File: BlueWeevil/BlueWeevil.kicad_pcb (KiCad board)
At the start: 2 copper layers, 370.5 x 94.4 mm, 256 parts, among them U1 Teensy_3.2, U2 AN32183A

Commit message: 1st pass at layout. Needs packages verified, and underglow LEDs added
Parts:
- removed the CHERRY at (331.0, 85.7)
- removed the CHERRY at (92.9, 85.7)
- removed the CHERRY at (335.8, 66.7)
- removed the REF** at (379.5, 76.5)
- removed the REF** at (314.3, 66.7)
- removed the REF** at (381.0, 67.3)
- removed the REF** at (375.3, 67.3)
- removed the REF** at (370.2, 67.3)
- removed the REF** at (361.3, 67.3)
- removed the REF** at (353.5, 75.4)
- removed the REF** at (74.9, 66.7)
- removed the REF** at (361.9, 28.6)
- removed the REF** at (362.6, 47.6)
- removed the REF** at (392.0, 76.5)
- removed the REF** at (358.8, 47.6)
- removed the REF** at (387.0, 76.5)
- removed the REF** at (203.8, 28.6)
- removed the REF** at (200.7, 66.7)
- removed the REF** at (397.0, 76.0)
- removed the REF** at (100.3, 47.6)
- removed the REF** at (76.8, 47.6)
- removed the REF** at (382.6, 47.5)
- removed the REF** at (266.8, 36.8)
- removed the REF** at (291.2, 36.8)
- removed the REF** at (299.7, 76.2)
- removed the REF** at (292.0, 96.2)
- removed the REF** at (336.0, 109.5)
- removed the REF** at (246.8, 97.2)
- removed the REF** at (73.7, 28.6)
- removed the REF** at (396.2, 85.1)
- added C10: 18pF, Capacitors_SMD:C_0805_HandSoldering, B.Cu at (371.6, 62.7)
- added C11: 1µF, Capacitors_SMD:C_0805_HandSoldering, B.Cu at (360.7, 54.6)
- added C12: 0.1µF, Capacitors_SMD:C_0805_HandSoldering, B.Cu at (349.5, 63.0)
- added C2: 0.1µF, Capacitors_SMD:C_0805_HandSoldering, B.Cu at (208.0, 58.2)
- added C3: 0.1µF, Capacitors_SMD:C_0805_HandSoldering, B.Cu at (194.1, 65.3)
- added C4: 10µF, Capacitors_Tantalum_SMD:TantalC_SizeA_EIA-3216_HandSoldering, B.Cu at (349.2, 33.3)
- added C5: 0.1µF, Capacitors_SMD:C_0805_HandSoldering, B.Cu at (349.5, 68.6)
- added C6: 0.1µF, Capacitors_SMD:C_0805_HandSoldering, B.Cu at (362.2, 73.9)
- added C7: 0.1µF, Capacitors_SMD:C_0805_HandSoldering, B.Cu at (367.8, 59.9)
- added C8: 0.1µF, Capacitors_SMD:C_0805_HandSoldering, B.Cu at (360.7, 56.6)
- added C9: 18pF, Capacitors_SMD:C_0805_HandSoldering, B.Cu at (371.6, 67.8)
- added F1: FP_Small, Fuse_Holders_and_Fuses:Fuse_SMD1206_HandSoldering, B.Cu at (352.6, 33.3)
- added J1: USB_OTG, Connect:USB_Mini-B, B.Cu at (358.2, 23.0)
- added R5: 120Ω, Resistors_SMD:R_0805_HandSoldering, B.Cu at (389.9, 89.9)
- added R6: 22, Resistors_SMD:R_0805_HandSoldering, B.Cu at (354.9, 55.2)
- added R7: 22, Resistors_SMD:R_0805_HandSoldering, B.Cu at (356.5, 55.2)
- added R8: 10k, Resistors_SMD:R_0805_HandSoldering, B.Cu at (387.1, 59.9)
- added REF**: GND Via, Cherry:GNDVia, F.Cu at (313.9, 63.2)
- added REF**: GND Via, Cherry:GNDVia, F.Cu at (314.7, 85.3)
- added REF**: GND Via, Cherry:GNDVia, F.Cu at (314.7, 91.2)
- added REF**: GND Via, Cherry:GNDVia, F.Cu at (305.6, 91.2)
- added REF**: GND Via, Cherry:GNDVia, F.Cu at (313.9, 71.4)
- added REF**: GND Via, Cherry:GNDVia, F.Cu at (323.2, 71.1)
- added REF**: GND Via, Cherry:GNDVia, F.Cu at (363.2, 71.9)
- added REF**: GND Via, Cherry:GNDVia, F.Cu at (340.6, 90.7)
- added REF**: GND Via, Cherry:GNDVia, F.Cu at (359.7, 90.7)
- added REF**: GND Via, Cherry:GNDVia, F.Cu at (360.4, 85.3)
- added REF**: GND Via, Cherry:GNDVia, F.Cu at (340.6, 85.3)
- added REF**: GND Via, Cherry:GNDVia, F.Cu at (305.6, 85.1)
- added RP1: 4.7KΩ, Resistors_SMD:R_Array_Convex_4x1206, B.Cu at (198.8, 71.1)
- added SW1: SW_RST, Buttons_Switches_SMD:SW_SPST_EVQP0, B.Cu at (390.5, 66.7)
- added X1: 16Mhz, Crystals:Crystal_SMD_5032_4Pads, B.Cu at (368.2, 65.0)
- R1: value 39kΩ -> 100KΩ; footprint Resistors_SMD:R_1206_HandSoldering -> Resistors_SMD:R_0805_HandSoldering
- R2: value 150Ω -> 20KΩ; footprint Resistors_SMD:R_1206_HandSoldering -> Resistors_SMD:R_0805_HandSoldering; moved to B.Cu
- R3: value 120Ω -> 150Ω; footprint Resistors_SMD:R_1206_HandSoldering -> Resistors_SMD:R_0805_HandSoldering; moved to B.Cu
- R4: footprint Resistors_SMD:R_1206_HandSoldering -> Resistors_SMD:R_0805_HandSoldering; moved to B.Cu
- U1: value Teensy_3.2 -> IS31FL3731; footprint Cherry:Teensy3.2 -> Housings_SSOP:SSOP-28_5.3x10.2mm_Pitch0.65mm
- U2: value AN32183A -> ATMEGA32U4RC-A; footprint Housings_SSOP:SSOP-24_5.3x8.2mm_Pitch0.65mm -> Housings_QFP:TQFP-44_10x10mm_Pitch0.8mm
- moved R2 182.4 mm to (210.1, 58.1), turned to 270 degrees
- moved U1 160.5 mm to (199.9, 61.2), turned to 180 degrees
- moved R1 102.0 mm to (204.7, 75.7)
- moved C1 101.8 mm to (206.0, 58.2), turned to 270 degrees
- moved U2 54.5 mm to (357.7, 65.7), turned to 270 degrees
- moved D51 30.2 mm to (342.9, 74.9), turned to 180 degrees
- moved D45 23.7 mm to (220.0, 74.7), turned to 180 degrees
- moved D35 21.4 mm to (379.1, 55.6), turned to 180 degrees
- moved D17 18.5 mm to (381.0, 23.5)
- moved D21 17.9 mm to (94.6, 42.2)
- moved D39 17.2 mm to (100.3, 74.7)
- moved D12 15.6 mm to (243.3, 33.0), turned to 90 degrees
- moved R4 13.8 mm to (389.9, 92.2)
- moved R3 12.7 mm to (389.9, 80.5)
- moved D78 4.83 mm to (381.5, 99.3), turned to 270 degrees
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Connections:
- C1 pad 1: Net-(C1-Pad1) -> +5V
- D17 pad 1: Net-(D17-Pad1) -> R10
- D18 pad 1: Net-(D17-Pad1) -> R10
- D19 pad 1: R2 -> R2/SCK
- D20 pad 1: R2 -> R2/SCK
- D21 pad 1: R2 -> R2/SCK
- D22 pad 1: R2 -> R2/SCK
- D23 pad 1: R2 -> R2/SCK
- D24 pad 1: R2 -> R2/SCK
- D25 pad 1: R2 -> R2/SCK
- D26 pad 1: R2 -> R2/SCK
- D35 pad 1: Net-(D17-Pad1) -> R10
- D36 pad 1: Net-(D17-Pad1) -> R10
- D37 pad 1: R3 -> R3/MOSI
- D38 pad 1: R3 -> R3/MOSI
- D39 pad 1: R3 -> R3/MOSI
- D40 pad 1: R3 -> R3/MOSI
- D41 pad 1: R3 -> R3/MOSI
- D42 pad 1: R3 -> R3/MOSI
- D43 pad 1: R3 -> R3/MOSI
- D44 pad 1: R3 -> R3/MOSI
- D52 pad 1: R4 -> R4/MISO
- D53 pad 1: R4 -> R4/MISO
- D54 pad 1: R4 -> R4/MISO
- D55 pad 1: R4 -> R4/MISO
- D56 pad 1: R4 -> R4/MISO
- D57 pad 1: R4 -> R4/MISO
- D58 pad 1: R4 -> R4/MISO
- D59 pad 1: R4 -> R4/MISO
- D78 pad 2: Net-(D17-Pad1) -> Net-(D78-Pad2)
- R1 pad 1: Net-(R1-Pad1) -> LED_NSRT
- R2 pad 2: Net-(R2-Pad2) -> GND
- R3 pad 2: Net-(R3-Pad2) -> PWM_RED
- R4 pad 2: Net-(R4-Pad2) -> PWM_GREEN
- RGB1 pad 2: Net-(R4-Pad1) -> Net-(R3-Pad1)
- RGB1 pad 3: Net-(R3-Pad1) -> Net-(R4-Pad1)
- RGB1 pad 4: Net-(R2-Pad1) -> Net-(R5-Pad1)
- SW_A_40 pad A: Z4 -> CA4
- SW_A_40 pad K: Z6 -> CA3
- SW_Alt_71 pad A: Z8 -> CA5
- SW_Alt_71 pad K: Z9 -> CA6
- SW_Alt_73 pad A: Z1 -> CB1
- SW_Alt_73 pad K: Z10 -> CB6
- SW_B_59 pad A: Z5 -> CA8
- SW_B_59 pad K: Z8 -> CA4
- SW_Backspace_16 pad A: Z7 -> CB8
- SW_Backspace_16 pad K: Z2 -> CB1
- SW_C_57 pad A: Z3 -> CA6
- SW_C_57 pad K: Z8 -> CA4
- SW_Caps_39 pad A: Z3 -> CA3
- SW_Caps_39 pad K: Z6 -> CA4
- SW_Ctrl_69 pad A: Z6 -> CA3
- SW_Ctrl_69 pad K: Z9 -> CA6
- SW_D_42 pad A: Z6 -> CA6
- SW_D_42 pad K: Z5 -> CA3
- SW_Del_35 pad A: Z8 -> CB8
- SW_Del_35 pad K: Z4 -> CB5
- SW_E_24 pad A: Z6 -> CA6
- SW_E_24 pad K: Z3 -> CA2
- SW_Enter_51 pad A: Z6 -> CB7
- SW_Enter_51 pad K: Z7 -> CB3
- SW_F10_68 pad A: Z5 -> CA2
- SW_F10_68 pad K: Z9 -> CA6
- SW_F1_1 pad A: Z1 -> CA1
- SW_F1_1 pad K: Z2 -> CA2
- SW_F2_2 pad A: Z2 -> CA2
- SW_F2_2 pad K: Z1 -> CA1
- SW_F3_19 pad A: Z1 -> CA1
- SW_F3_19 pad K: Z4 -> CA3
- SW_F4_20 pad A: Z2 -> CA2
- SW_F4_20 pad K: Z4 -> CA3
- SW_F5_37 pad A: Z1 -> CA1
- SW_F5_37 pad K: Z6 -> CA4
- SW_F6_38 pad A: Z2 -> CA2
- SW_F6_38 pad K: Z6 -> CA4
- SW_F7_52 pad A: Z7 -> CA1
- SW_F7_52 pad K: Z6 -> CA5
- SW_F8_53 pad A: Z8 -> CA2
- SW_F8_53 pad K: Z6 -> CA5
- SW_F9_67 pad A: Z4 -> CA1
- SW_F9_67 pad K: Z9 -> CA6
- SW_F_43 pad A: Z7 -> CA7
- SW_F_43 pad K: Z5 -> CA3
- SW_G_44 pad A: Z8 -> CA8
- SW_G_44 pad K: Z5 -> CA3
- SW_H_45 pad A: Z9 -> CB1
- SW_H_45 pad K: Z5 -> CB4
- SW_I_29 pad A: Z2 -> CB3
- SW_I_29 pad K: Z5 -> CB2
- SW_Ins_17 pad A: Z8 -> CB7
- SW_Ins_17 pad K: Z2 -> CB5
- SW_J_46 pad A: Z1 -> CB2
- SW_J_46 pad K: Z7 -> CB4
- SW_K_47 pad A: Z2 -> CB3
- SW_K_47 pad K: Z7 -> CB4
- SW_L_48 pad A: Z3 -> CB4
- SW_L_48 pad K: Z7 -> CB3
- SW_M_61 pad A: Z7 -> CB2
- SW_M_61 pad K: Z8 -> CB5
- SW_Menu_75 pad A: Z3 -> CB3
- SW_Menu_75 pad K: Z10 -> CB6
- SW_N_60 pad A: Z6 -> CB1
- SW_N_60 pad K: Z8 -> CB5
- SW_O_30 pad A: Z3 -> CB4
- SW_O_30 pad K: Z5 -> CB2
- SW_P_31 pad A: Z4 -> CB5
- SW_P_31 pad K: Z5 -> CB2
- SW_PgDn_36 pad A: Z9 -> CB8
- SW_PgDn_36 pad K: Z4 -> CB3
- SW_PgUp_18 pad A: Z9 -> CB8
- SW_PgUp_18 pad K: Z2 -> CB4
- SW_Q_22 pad A: Z4 -> CA4
- SW_Q_22 pad K: Z3 -> CA2
- SW_R_25 pad A: Z7 -> CA7
- SW_R_25 pad K: Z3 -> CA2
- SW_S_41 pad A: Z5 -> CA5
- SW_S_41 pad K: Z6 -> CA3
- SW_Shift_54 pad A: Z9 -> CA3
- SW_Shift_54 pad K: Z6 -> CA5
- SW_Shift_65 pad A: Z2 -> CB6
- SW_Shift_65 pad K: Z9 -> CB4
- SW_T_26 pad A: Z8 -> CA8
- SW_T_26 pad K: Z3 -> CA2
- SW_Tab_21 pad A: Z3 -> CA3
- SW_Tab_21 pad K: Z4 -> CA2
- SW_U_28 pad A: Z1 -> CB2
- SW_U_28 pad K: Z5 -> CB3
- SW_V_58 pad A: Z4 -> CA7
- SW_V_58 pad K: Z8 -> CA4
- SW_W_23 pad A: Z5 -> CA5
- SW_W_23 pad K: Z3 -> CA2
- SW_Win_70 pad A: Z7 -> CA4
- SW_Win_70 pad K: Z9 -> CA6
- SW_Win_74 pad A: Z2 -> CB2
- SW_Win_74 pad K: Z10 -> CB6
- SW_X10Y1_9 pad A: Z9 -> CB1
- SW_X10Y1_9 pad K: Z1 -> CB2
- SW_X11Y1_10 pad A: Z1 -> CB2
- SW_X11Y1_10 pad K: Z3 -> CB1
- SW_X12Y1_11 pad A: Z2 -> CB3
- SW_X12Y1_11 pad K: Z3 -> CB1
- SW_X13Y1_12 pad A: Z3 -> CB4
- SW_X13Y1_12 pad K: Z2 -> CB1
- SW_X13Y4_62 pad A: Z8 -> CB3
- SW_X13Y4_62 pad K: Z7 -> CB5
- SW_X14Y1_13 pad A: Z4 -> CB5
- SW_X14Y1_13 pad K: Z2 -> CB1
- SW_X14Y4_63 pad A: Z9 -> CB4
- SW_X14Y4_63 pad K: Z7 -> CB5
- SW_X15Y1_14 pad A: Z5 -> CB6
- SW_X15Y1_14 pad K: Z2 -> CB1
- SW_X15Y2_32 pad A: Z5 -> CB6
- SW_X15Y2_32 pad K: Z4 -> CB2
- SW_X15Y3_49 pad A: Z4 -> CB5
- SW_X15Y3_49 pad K: Z7 -> CB3
- SW_X15Y4_64 pad A: Z1 -> CB5
- SW_X15Y4_64 pad K: Z9 -> CB4
- SW_X16Y1_15 pad A: Z6 -> CB7
- SW_X16Y1_15 pad K: Z2 -> CB1
- SW_X16Y2_33 pad A: Z6 -> CB7
- SW_X16Y2_33 pad K: Z4 -> CB2
- SW_X16Y3_50 pad A: Z5 -> CB6
- SW_X16Y3_50 pad K: Z7 -> CB3
- SW_X17Y2_34 pad A: Z7 -> CB8
- SW_X17Y2_34 pad K: Z4 -> CB2
- SW_X18Y5_76 pad A: Z4 -> CB4
- SW_X18Y5_76 pad K: Z10 -> CB6
- SW_X19Y4_66 pad A: Z3 -> CB7
- SW_X19Y4_66 pad K: Z9 -> CB4
- SW_X19Y5_77 pad A: Z5 -> CB5
- SW_X19Y5_77 pad K: Z10 -> CB6
- SW_X20Y5_78 pad A: Z6 -> CB6
- SW_X20Y5_78 pad K: Z10 -> CB5
- SW_X20Y5_78 pad SW2: Net-(D17-Pad1) -> Net-(D78-Pad2)
- SW_X4Y1_3 pad A: Z3 -> CA3
- SW_X4Y1_3 pad K: Z1 -> CA1
- SW_X5Y1_4 pad A: Z4 -> CA4
- SW_X5Y1_4 pad K: Z1 -> CA1
- SW_X6Y1_5 pad A: Z5 -> CA5
- SW_X6Y1_5 pad K: Z1 -> CA1
- SW_X7Y1_6 pad A: Z6 -> CA6
- SW_X7Y1_6 pad K: Z1 -> CA1
- SW_X8Y1_7 pad A: Z7 -> CA7
- SW_X8Y1_7 pad K: Z1 -> CA1
- SW_X8Y5_72 pad A: Z9 -> CA6
- SW_X8Y5_72 pad K: Z8 -> CA5
- SW_X9Y1_8 pad A: Z8 -> CA8
- SW_X9Y1_8 pad K: Z1 -> CA1
- SW_X_56 pad A: Z2 -> CA5
- SW_X_56 pad K: Z8 -> CA4
- SW_Y_27 pad A: Z9 -> CB1
- SW_Y_27 pad K: Z3 -> CB3
- SW_Z_55 pad A: Z1 -> CA4
- SW_Z_55 pad K: Z8 -> CA5
- U1 pad 1: C2 -> CA9
- U1 pad 10: R3 -> CB4
- U1 pad 11: R4 -> CB5
- U1 pad 12: R5 -> CB6
- U1 pad 13: R6 -> CB7
- U1 pad 14: R7 -> CB8
- U1 pad 15: R8 -> CB9
- U1 pad 16: R9 -> Net-(C3-Pad1)
- U1 pad 17: R10 -> (no net)
- U1 pad 18: SDA -> GND
- U1 pad 19: SCL -> LED_SDA
- U1 pad 2: C3 -> +5V
- U1 pad 20: NSRT -> LED_SCL
- U1 pad 21: Net-(R2-Pad2) -> CA1
- U1 pad 22: Net-(R3-Pad2) -> CA2
- U1 pad 23: Net-(R4-Pad2) -> CA3
- U1 pad 3: C4 -> LED_NSRT
- U1 pad 4: C5 -> Net-(RP1-Pad8)
- U1 pad 5: C6 -> GND
- U1 pad 6: C7 -> Net-(R2-Pad1)
- U1 pad 7: C8 -> CB1
- U1 pad 8: R1 -> CB2
- U1 pad 9: R2 -> CB3
- U2 pad 1: Net-(C1-Pad1) -> (no net)
- U2 pad 10: Z7 -> R3/MOSI
- U2 pad 11: Z6 -> R4/MISO
- U2 pad 12: Z5 -> PWM_BLUE
- U2 pad 13: Net-(C1-Pad1) -> RST
- U2 pad 14: Z4 -> +5V
- U2 pad 16: Z3 -> Net-(C10-Pad1)
- U2 pad 17: +5V -> Net-(C9-Pad1)
- U2 pad 18: Z2 -> LED_SCL
- U2 pad 19: Z1 -> LED_SDA
- U2 pad 2: SCL -> +5V
- U2 pad 20: (no net) -> C3
- U2 pad 21: (no net) -> C4
- U2 pad 22: NSRT -> C6
- U2 pad 24: Net-(R1-Pad1) -> +5V
- U2 pad 3: SDA -> D-
- U2 pad 4: GND -> D+
- U2 pad 5: Z10 -> GND
- U2 pad 6: Z9 -> Net-(C11-Pad1)
- U2 pad 8: Z8 -> R1
- U2 pad 9: GND -> R2/SCK
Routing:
- net C6: track 0.00 -> 503.8 mm, vias 0 -> 6
- net C7: track 0.00 -> 503.3 mm, vias 0 -> 4
- net C1: track 0.00 -> 495.9 mm, vias 0 -> 2
- net C5: track 0.00 -> 493.7 mm, vias 0 -> 5
- net C4: track 0.00 -> 492.7 mm, vias 0 -> 5
- net C3: track 0.00 -> 491.7 mm, vias 0 -> 5
- net C2: track 0.00 -> 461.6 mm, vias 0 -> 1
- net C8: track 0.00 -> 441.7 mm, vias 0 -> 7
- net CB5: track 0.00 -> 387.4 mm, vias 0 -> 3
- net R1: track 0.00 -> 381.6 mm, vias 0 -> 4
- net R4/MISO: track 0.00 -> 365.2 mm, vias 0 -> 2
- net CB3: track 0.00 -> 364.4 mm, vias 0 -> 5
- net R3/MOSI: track 0.00 -> 360.4 mm, vias 0 -> 2
- net R2/SCK: track 0.00 -> 356.1 mm, vias 0 -> 3
- net CB7: track 0.00 -> 355.1 mm, vias 0 -> 6
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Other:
- net class Default: clearance 0.1524 -> 0.2032
- rule trace_clearance: 0.1524 -> 0.2032
- rule trace_min: 0.01524 -> 0.2032
- rule via_min_size: 0.03048 -> 0.6096

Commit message: RGB LEDs placed
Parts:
- added RGB10: Led_RGB_CA, Cherry:SMP4-RGB, B.Cu at (31.8, 66.7)
- added RGB11: Led_RGB_CA, Cherry:SMP4-RGB, B.Cu at (90.9, 22.1)
- added RGB12: Led_RGB_CA, Cherry:SMP4-RGB, B.Cu at (152.0, 22.1)
- added RGB13: Led_RGB_CA, Cherry:SMP4-RGB, B.Cu at (152.7, 110.5)
- added RGB14: Led_RGB_CA, Cherry:SMP4-RGB, B.Cu at (214.4, 110.5)
- added RGB15: Led_RGB_CA, Cherry:SMP4-RGB, B.Cu at (90.9, 110.5)
- added RGB20: Led_RGB_CA, Cherry:SMP4-RGB, B.Cu at (277.4, 22.1)
- added RGB21: Led_RGB_CA, Cherry:SMP4-RGB, B.Cu at (397.0, 66.3)
- added RGB22: Led_RGB_CA, Cherry:SMP4-RGB, B.Cu at (335.9, 110.5)
- added RGB23: Led_RGB_CA, Cherry:SMP4-RGB, B.Cu at (219.7, 22.1)
- added RGB24: Led_RGB_CA, Cherry:SMP4-RGB, B.Cu at (330.2, 22.2)
- added RGB25: Led_RGB_CA, Cherry:SMP4-RGB, B.Cu at (281.2, 110.5)
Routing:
- net C6: track 503.8 -> 504.5 mm

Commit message: 100% Routed- Need to verify all packages, clean up labels and tracks.
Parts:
- removed the REF** at (215.4, 106.8)
- removed the REF** at (188.0, 104.8)
- added REF**: GND Via, Cherry:GNDVia, F.Cu at (198.8, 104.1)
- added REF**: GND Via, Cherry:GNDVia, F.Cu at (206.2, 111.0)
- added REF**: GND Via, Cherry:GNDVia, F.Cu at (213.1, 107.6)
- added REF**: GND Via, Cherry:GNDVia, F.Cu at (206.0, 100.6)
- moved RGB21 75.9 mm to (335.3, 110.5), turned to 90 degrees
- moved RGB22 75.4 mm to (397.0, 66.3)
- moved REF** 2.61 mm to (288.9, 105.9)
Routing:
- net CB9: track 0.00 -> 477.0 mm, vias 0 -> 9
- net CA9: track 0.00 -> 442.2 mm, vias 0 -> 8
- net CA8: track 96.7 -> 445.2 mm, vias 3 -> 11
- net CA7: track 98.7 -> 436.7 mm, vias 2 -> 8
- net CB8: track 296.0 -> 524.8 mm, vias 3 -> 10
- net CB7: track 355.1 -> 509.2 mm, vias 6 -> 13
- net CB5: track 387.4 -> 459.4 mm, vias 3 -> 5
- net CA3: track 264.0 -> 321.2 mm, vias 1 -> 2
- net CB2: track 336.6 -> 386.8 mm, vias 5 -> 7
- net CB4: track 342.5 -> 383.2 mm, vias 3 -> 5
- net CA2: track 267.0 -> 304.7 mm
- net CA4: track 307.2 -> 341.9 mm
- net CB3: track 364.4 -> 392.6 mm, vias 5 -> 7
- net CA5: track 349.8 -> 366.9 mm, vias 3 -> 4
- net CB1: track 321.5 -> 335.7 mm
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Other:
- board text removed: "/u/ca178858"

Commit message: Packages verified, BOM w/part numbers created
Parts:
- removed the REF** at (397.6, 25.2)
- removed RP1: 4.7KΩ, Resistors_SMD:R_Array_Convex_4x1206
- added R10: 4.7KΩ, Capacitors_SMD:C_0805_HandSoldering, B.Cu at (200.7, 71.8)
- added R9: 4.7KΩ, Capacitors_SMD:C_0805_HandSoldering, B.Cu at (200.7, 69.2)
- added REF**: GND Via, Cherry:GNDVia, F.Cu at (69.6, 29.7)
- added REF**: GND Via, Cherry:GNDVia, F.Cu at (97.8, 103.9)
- added REF**: GND Via, Cherry:GNDVia, F.Cu at (97.8, 110.0)
- added REF**: GND Via, Cherry:GNDVia, F.Cu at (327.7, 34.3)
- added REF**: GND Via, Cherry:GNDVia, F.Cu at (351.5, 41.4)
- added REF**: GND Via, Cherry:GNDVia, F.Cu at (361.7, 41.1)
- added REF**: GND Via, Cherry:GNDVia, F.Cu at (355.1, 47.2)
- added REF**: GND Via, Cherry:GNDVia, F.Cu at (350.5, 47.2)
- added REF**: GND Via, Cherry:GNDVia, F.Cu at (361.7, 47.2)
- added REF**: GND Via, Cherry:GNDVia, F.Cu at (345.9, 33.5)
- added REF**: GND Via, Cherry:GNDVia, F.Cu at (365.3, 32.8)
- added REF**: GND Via, Cherry:GNDVia, F.Cu at (71.4, 50.0)
- added REF**: GND Via, Cherry:GNDVia, F.Cu at (349.8, 23.4)
- added REF**: GND Via, Cherry:GNDVia, F.Cu at (365.3, 23.4)
- added REF**: GND Via, Cherry:GNDVia, F.Cu at (397.8, 22.1)
- added REF**: GND Via, Cherry:GNDVia, F.Cu at (397.8, 45.2)
- added REF**: GND Via, Cherry:GNDVia, F.Cu at (397.8, 61.7)
- added REF**: GND Via, Cherry:GNDVia, F.Cu at (348.0, 71.9)
- added REF**: GND Via, Cherry:GNDVia, F.Cu at (359.7, 75.2)
- added REF**: GND Via, Cherry:GNDVia, F.Cu at (348.0, 75.2)
- added REF**: GND Via, Cherry:GNDVia, F.Cu at (352.8, 71.9)
- added REF**: GND Via, Cherry:GNDVia, F.Cu at (359.7, 68.3)
- added REF**: GND Via, Cherry:GNDVia, F.Cu at (71.6, 69.1)
- added REF**: GND Via, Cherry:GNDVia, F.Cu at (359.7, 65.0)
- added REF**: GND Via, Cherry:GNDVia, F.Cu at (356.6, 62.7)
- added REF**: GND Via, Cherry:GNDVia, F.Cu at (286.0, 27.7)
- added REF**: GND Via, Cherry:GNDVia, F.Cu at (277.1, 33.0)
- added REF**: GND Via, Cherry:GNDVia, F.Cu at (100.1, 39.4)
- added REF**: GND Via, Cherry:GNDVia, F.Cu at (91.2, 39.1)
- added REF**: GND Via, Cherry:GNDVia, F.Cu at (94.2, 33.8)
- added REF**: GND Via, Cherry:GNDVia, F.Cu at (95.5, 22.6)
- added REF**: GND Via, Cherry:GNDVia, F.Cu at (94.8, 108.2)
- added REF**: GND Via, Cherry:GNDVia, F.Cu at (101.7, 93.2)
- moved REF** 4.87 mm to (274.6, 27.9)
- moved R1 4.30 mm to (200.7, 74.3), turned to 180 degrees
- moved REF** 2.30 mm to (300.5, 28.2)
- moved J1 1.57 mm to (357.0, 24.0)
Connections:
- U1 pad 4: Net-(RP1-Pad8) -> (no net)
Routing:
- net GND: track 313.5 -> 297.6 mm
- net Net-(RP1-Pad8): track 15.4 -> 0.00 mm, vias 2 -> 0
- net LED_SDA: track 196.0 -> 192.4 mm
- net R6: track 208.4 -> 211.6 mm
- net LED_NSRT: track 184.0 -> 180.8 mm
- net +5V: track 319.3 -> 317.0 mm, vias 9 -> 7
- net CA6: track 325.1 -> 323.0 mm
- net R2/SCK: track 356.1 -> 354.2 mm
- net USB-: track 28.6 -> 27.1 mm
- net CA8: track 445.2 -> 443.7 mm, vias 11 -> 10
- net CB2: track 386.8 -> 385.3 mm
- net USB+: track 28.1 -> 26.6 mm
- net Net-(F1-Pad1): track 6.40 -> 4.92 mm
- net C3: track 493.7 -> 495.0 mm
- net CB9: track 477.0 -> 478.2 mm
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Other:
- net class Default: clearance 0.2032 -> 0.1778
- rule trace_clearance: 0.2032 -> 0.1778

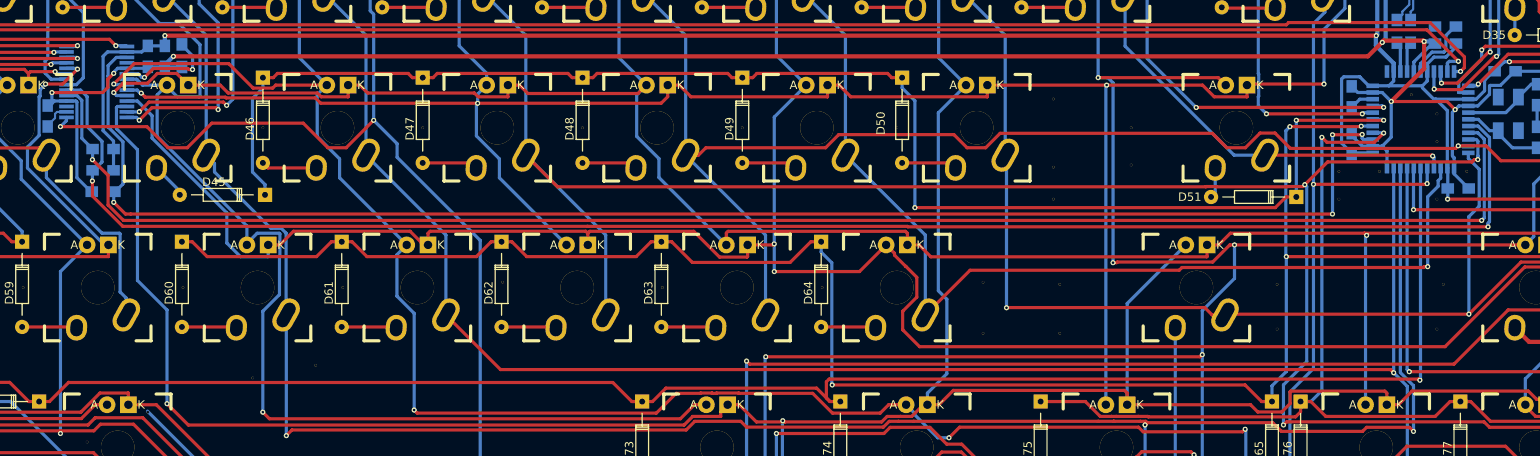
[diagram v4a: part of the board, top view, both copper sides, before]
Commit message: Fixed clearance issues.
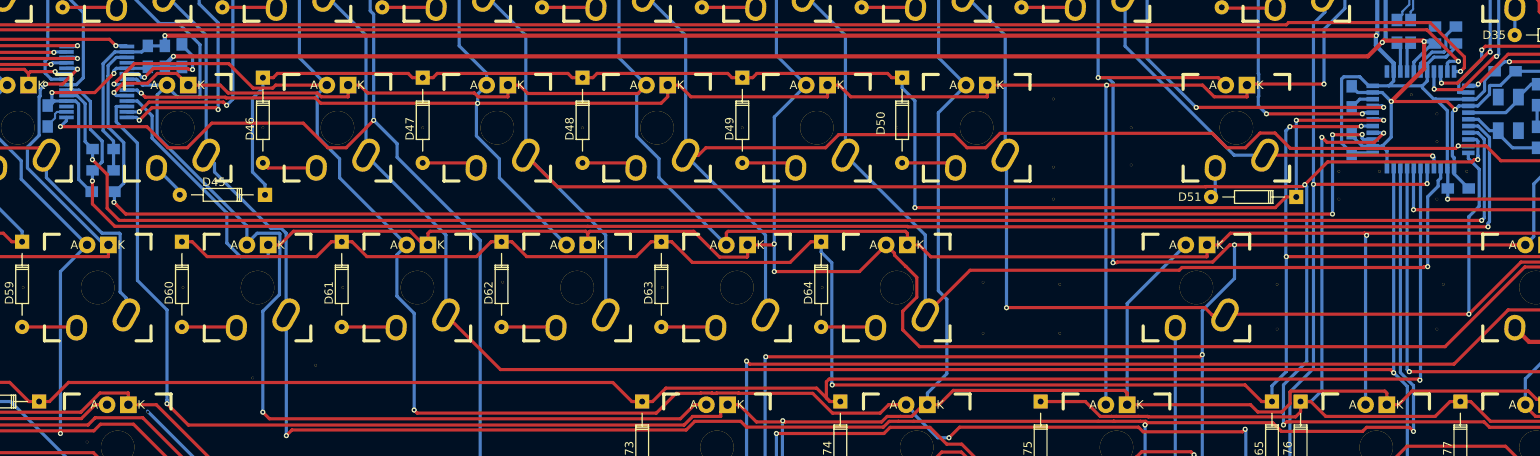
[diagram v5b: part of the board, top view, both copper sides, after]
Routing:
- net +5V: track 317.0 -> 316.5 mm
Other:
- net class Default: clearance 0.1778 -> 0.2032
- rule trace_clearance: 0.1778 -> 0.2032
